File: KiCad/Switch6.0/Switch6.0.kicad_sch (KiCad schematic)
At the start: 20 parts, among them Q1 BD139, Q2 IXTH90P10P, Q4 BD139, Q5A1 BSC340N08NS3G, Q6 BD139

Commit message: new upload.
correct versions
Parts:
- D1, D8: footprint Diode_SMD:D_SOD-523 -> Library:D_SOD-523_new
- renumbered V58 to VTackt1
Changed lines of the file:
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@@
   (symbol (lib_id "Connector_Generic:Conn_01x01") (at 71.12 80.01 180) (unit 1)
     (in_bom yes) (on_board yes) (fields_autoplaced)
-    (property "Reference" "V58" (id 0) (at 71.12 73.66 0))
+    (property "Reference" "VTackt1" (id 0) (at 71.12 73.66 0))
     (property "Value" "Conn_01x01" (id 1) (at 71.12 76.2 0))
     (property "Footprint" "Connector:Banana_Jack_1Pin" (id 2) (at 71.12 80.01 0)
@@
       (effects (font (size 1.27 1.27)) (justify right))
     )
-    (property "Footprint" "Diode_SMD:D_SOD-523" (id 2) (at 144.78 109.22 0)
+    (property "Footprint" "Library:D_SOD-523_new" (id 2) (at 144.78 109.22 0)
       (effects (font (size 1.27 1.27)) hide)
     )
@@
     (property "Reference" "D1" (id 0) (at 107.95 64.77 0))
     (property "Value" "BAT54XV2T5G" (id 1) (at 107.95 67.31 0))
-    (property "Footprint" "Diode_SMD:D_SOD-523" (id 2) (at 107.95 71.12 0)
+    (property "Footprint" "Library:D_SOD-523_new" (id 2) (at 107.95 71.12 0)
       (effects (font (size 1.27 1.27)) hide)
     )
@@
     )
     (path "/d73b824c-b3b6-4063-b940-a86ee2bf0204"
-      (reference "D1") (unit 1) (value "BAT54XV2T5G") (footprint "Diode_SMD:D_SOD-523")
+      (reference "D1") (unit 1) (value "BAT54XV2T5G") (footprint "Library:D_SOD-523_new")
     )
     (path "/bf88f533-a4f9-4f1e-9654-670f7fbb62bb"
-      (reference "D8") (unit 1) (value "BAT54XV2T5G") (footprint "Diode_SMD:D_SOD-523")
+      (reference "D8") (unit 1) (value "BAT54XV2T5G") (footprint "Library:D_SOD-523_new")
     )
     (path "/f9ad1dc2-f892-4f68-ab24-4b655bfddfdd"
@@
     )
     (path "/16f870ba-2f0a-423c-93f7-b68a39f617e3"
-      (reference "V58") (unit 1) (value "Conn_01x01") (footprint "Connector:Banana_Jack_1Pin")
+      (reference "VTackt1") (unit 1) (value "Conn_01x01") (footprint "Connector:Banana_Jack_1Pin")
     )
     (path "/6c1044d2-7ea5-4cdc-815d-7e2935d72573"

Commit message: Final results
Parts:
- added C10, C11, C2, C3, C4, C5, C6, C7, C8, C9: 0.1uF, Capacitor_SMD:C_0805_2012Metric, symbol Device:C
- added Q_D1, Q_G1, Q_G2, Q_Masse1, Q_S1: Conn_01x01, Connector_PinHeader_2.54mm:PinHeader_1x01_P2.54mm_Vertical, symbol Connector_Generic:Conn_01x01
- added R10, R11, R12, R3, R4, R5, R6, R7, R8, R9: 2R2, Resistor_SMD:R_2512_6332Metric, symbol Device:R
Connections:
- net 56V: now also Q_S1.1 (Pin_1), R10.1, R11.1, R12.1, R3.1, R4.1, R5.1, R6.1, R7.1, R8.1, R9.1
- net D: now also Q_D1.1 (Pin_1)
- net GND: now also C10.2, C11.2, C2.2, C3.2, C4.2, C5.2, C6.2, C7.2, C8.2, C9.2, Q_Masse1.1 (Pin_1)
- net G2: now reaches D8.2 (K), Q5A1.4 (G), Q6.2 (C), R22.2, R58.2, R59.2
- net G2: now also Q_G2.1 (Pin_1)
- net G1: now reaches D1.1 (A), Q1.1 (E), Q2.2 (G)
- net G1: now also Q_G1.1 (Pin_1)
- new net: C10.1, R11.2
- new net: C7.1, R8.2
- new net: C6.1, R7.2
- new net: C4.1, R5.2
- new net: C2.1, R3.2
- new net: C3.1, R4.2
- new net: C11.1, R12.2
- new net: C5.1, R6.2
- new net: C8.1, R9.2
- new net: C9.1, R10.2
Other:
- moved on the sheet: C18, D1, D8, GNDall1, Q1, Q2, Q4, Q5A1, Q6, R19, R2, R22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

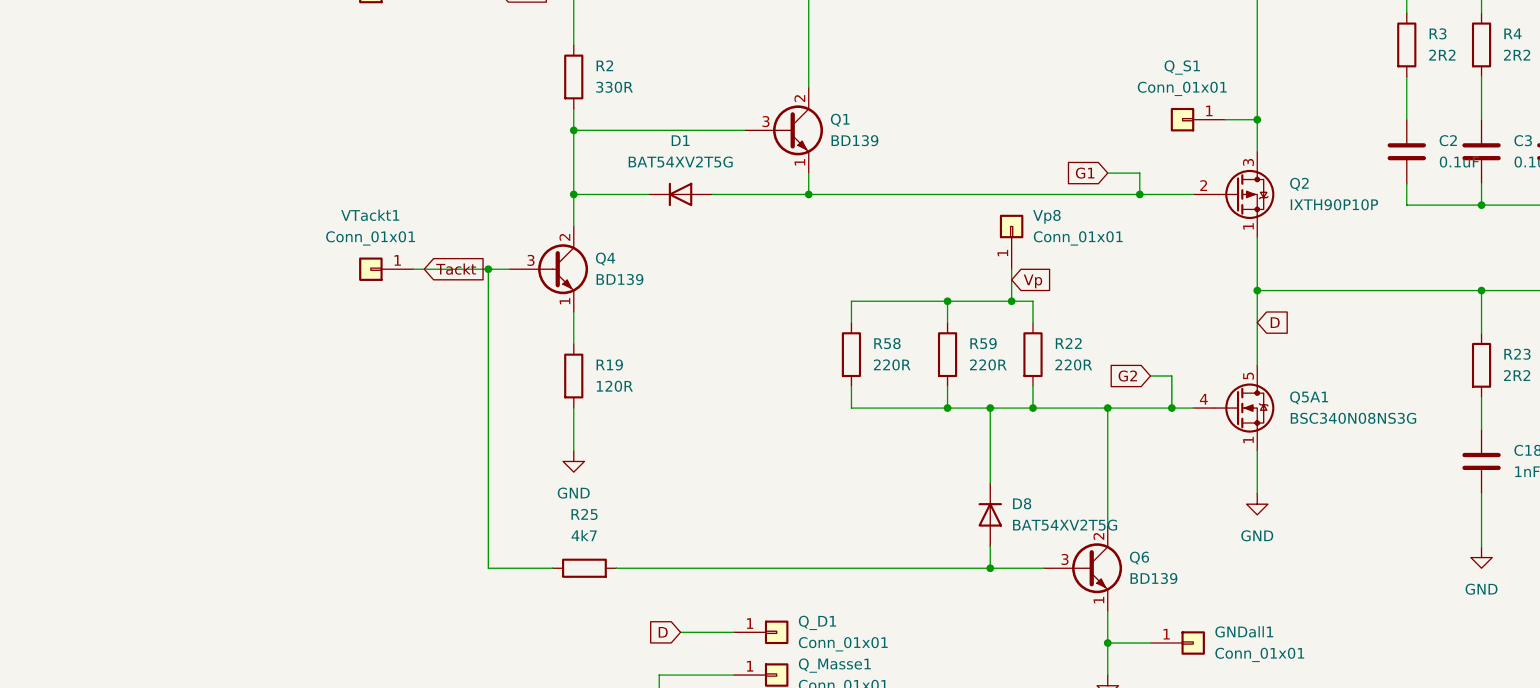
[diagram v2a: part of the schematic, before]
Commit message: Simulation and Kicad update
Simulation oof the Switch updated with an op amp. Kicad structure updated (0.2 version)
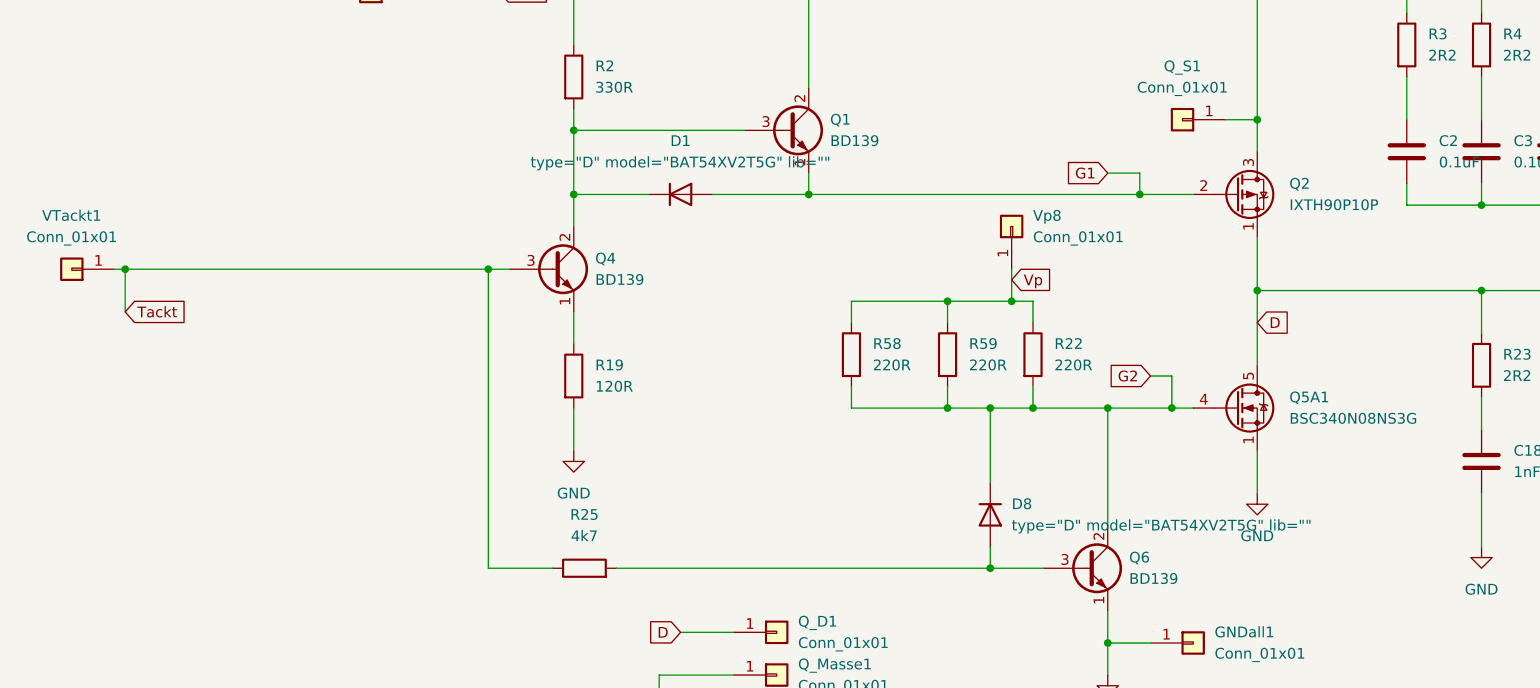
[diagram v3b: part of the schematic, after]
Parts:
- D1, D8: value BAT54XV2T5G -> ${SIM.PARAMS}; Spice_Netlist_Enabled Y -> (none); Spice_Primitive D -> (none)
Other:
- moved on the sheet: VTackt1

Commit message: Switch Platine
Platine 0.2 Entwurf mit OpV
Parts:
- added R1.1: 10k, Resistor_SMD:R_0805_2012Metric, symbol Device:R
- added R1.2: 2k, Resistor_SMD:R_0805_2012Metric, symbol Device:R
- added U1: AD8033, Package_SO:SOIC-8_3.9x4.9mm_P1.27mm, symbol Amplifier_Operational:AD8001AR
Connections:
- net 56V: now also U1.7 (V+)
- net GND: now also R1.2.2, U1.4 (V-)
- net Tackt: now also U1.3 (+); no longer Q4.3 (B), R25.1
- new net: Q4.3 (B), R1.1.1, R25.1, U1.6
- new net: R1.1.2, R1.2.1, U1.2 (-)
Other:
- moved on the sheet: C10, C11, C18, C2, C3, C4, C5, C6, C7, C8, C9, D1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
